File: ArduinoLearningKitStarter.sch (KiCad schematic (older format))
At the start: 83 parts, among them J1 USB_OTG, J10 DHT11, J2 CONN_01X08, J3 CONN_01X06, J4 CONN_01X08, J5 CONN_01X10, J6 I2C, J7 CONN_01X04, J8 CONN_01X02, J9 SPI, SW1 SW_PUSH, SW2 SW_PUSH, SW3 SW_PUSH, U1 arduino_nano, U2 arduino_uno, U3 ESP32-DEVKIT-C

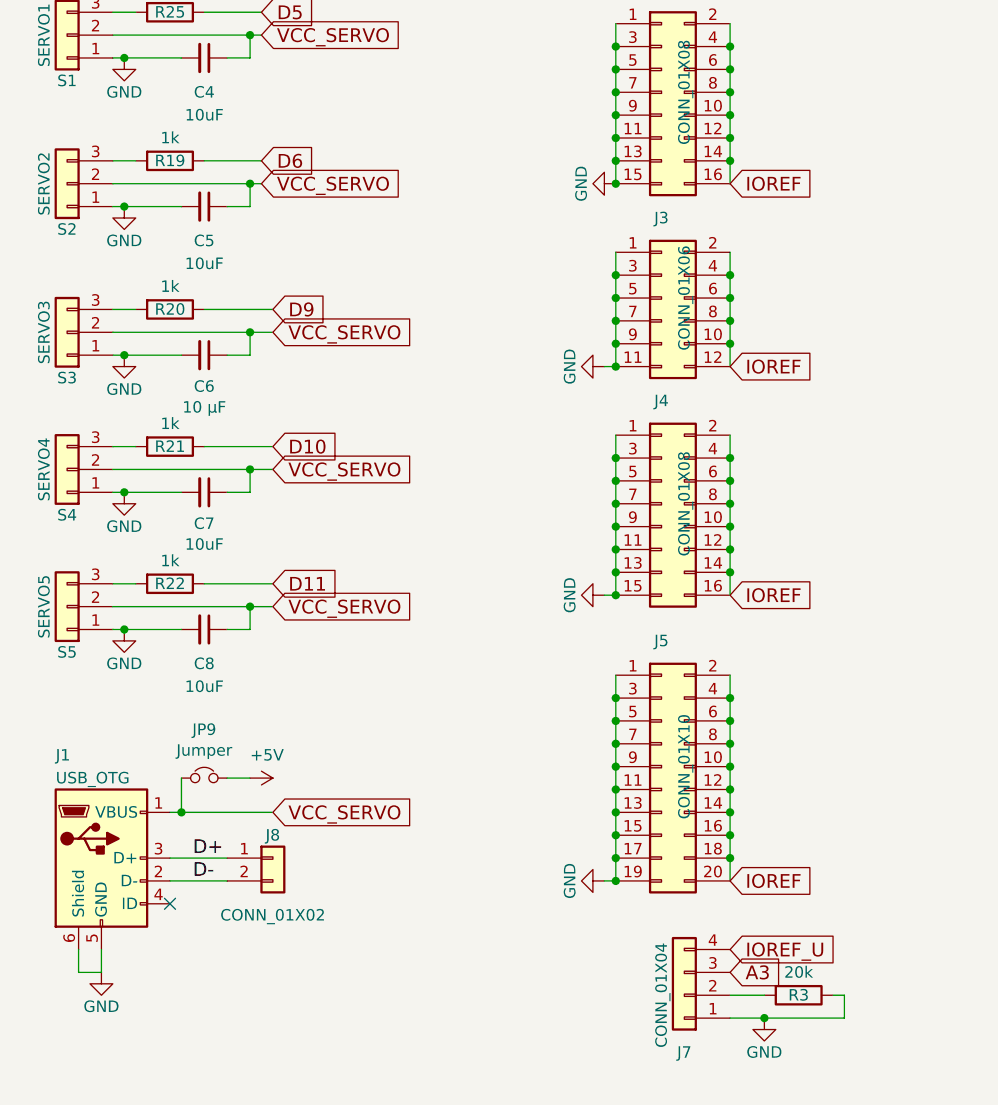
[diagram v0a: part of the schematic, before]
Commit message: Add connector for servo power supply
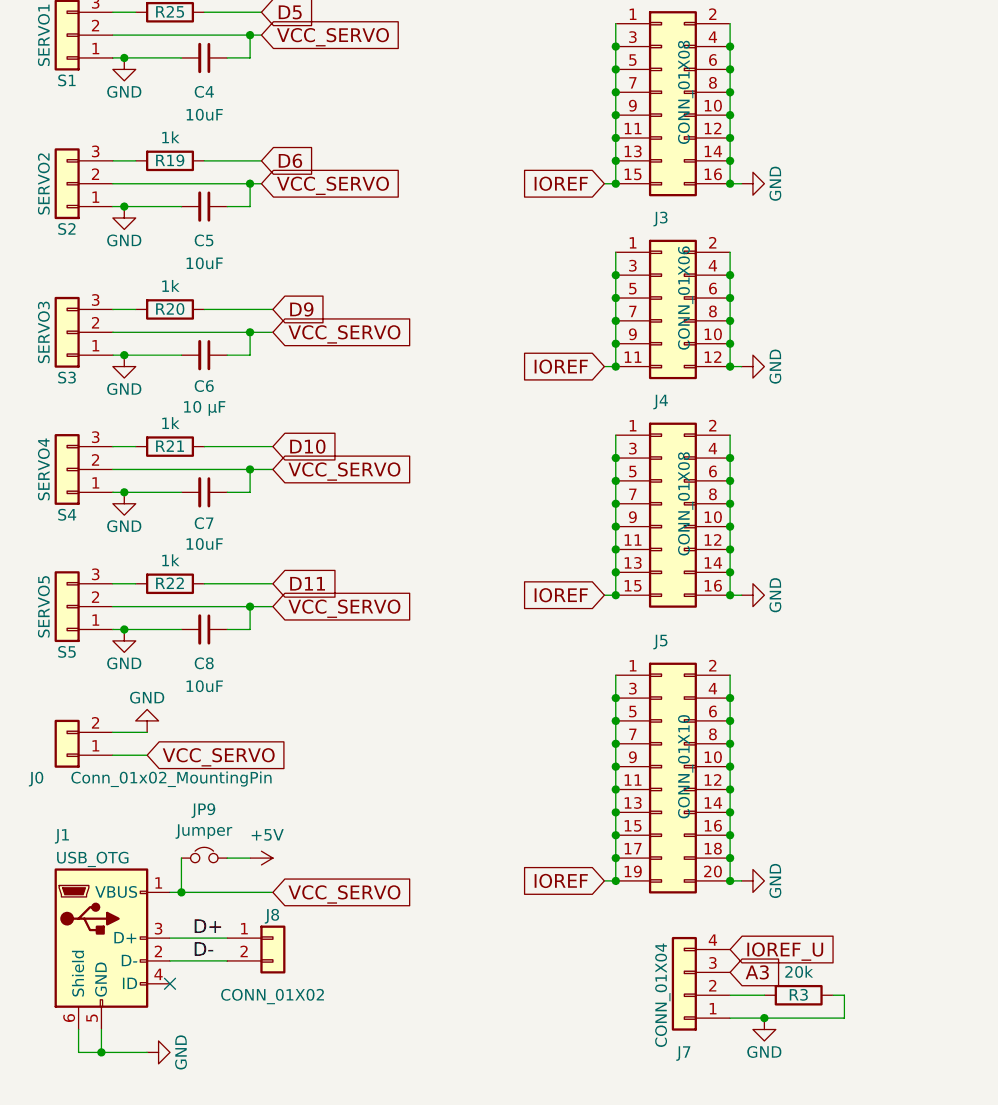
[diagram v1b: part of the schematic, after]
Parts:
- added J0: Conn_01x02_MountingPin, ALKS:2_pads_5mm, symbol ArduinoLearningKitStarter:Conn_01x02
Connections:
- net GND: now also J2.10 (Pin_10), J2.12 (Pin_12), J2.14 (Pin_14), J2.16 (Pin_16), J2.2 (Pin_2), J2.4 (Pin_4), J2.6 (Pin_6), J2.8 (Pin_8), J3.10 (Pin_10), J3.12 (Pin_12), J3.2 (Pin_2), J3.4 (Pin_4), J3.6 (Pin_6), J3.8 (Pin_8), J4.10 (Pin_10), J4.12 (Pin_12), J4.14 (Pin_14), J4.16 (Pin_16), J4.2 (Pin_2), J4.4 (Pin_4), J4.6 (Pin_6), J4.8 (Pin_8), J5.10 (Pin_10), J5.12 (Pin_12), J5.14 (Pin_14), J5.16 (Pin_16), J5.18 (Pin_18), J5.2 (Pin_2), J5.20 (Pin_20), J5.4 (Pin_4), J5.6 (Pin_6), J5.8 (Pin_8), J0.2 (Pin_2); no longer J2.1 (Pin_1), J2.11 (Pin_11), J2.13 (Pin_13), J2.15 (Pin_15), J2.3 (Pin_3), J2.5 (Pin_5), J2.7 (Pin_7), J2.9 (Pin_9), J3.1 (Pin_1), J3.11 (Pin_11), J3.3 (Pin_3), J3.5 (Pin_5), J3.7 (Pin_7), J3.9 (Pin_9), J4.1 (Pin_1), J4.11 (Pin_11), J4.13 (Pin_13), J4.15 (Pin_15), J4.3 (Pin_3), J4.5 (Pin_5), J4.7 (Pin_7), J4.9 (Pin_9), J5.1 (Pin_1), J5.11 (Pin_11), J5.13 (Pin_13), J5.15 (Pin_15), J5.17 (Pin_17), J5.19 (Pin_19), J5.3 (Pin_3), J5.5 (Pin_5), J5.7 (Pin_7), J5.9 (Pin_9)
- net IOREF: now also J2.1 (Pin_1), J2.11 (Pin_11), J2.13 (Pin_13), J2.15 (Pin_15), J2.3 (Pin_3), J2.5 (Pin_5), J2.7 (Pin_7), J2.9 (Pin_9), J3.1 (Pin_1), J3.11 (Pin_11), J3.3 (Pin_3), J3.5 (Pin_5), J3.7 (Pin_7), J3.9 (Pin_9), J4.1 (Pin_1), J4.11 (Pin_11), J4.13 (Pin_13), J4.15 (Pin_15), J4.3 (Pin_3), J4.5 (Pin_5), J4.7 (Pin_7), J4.9 (Pin_9), J5.1 (Pin_1), J5.11 (Pin_11), J5.13 (Pin_13), J5.15 (Pin_15), J5.17 (Pin_17), J5.19 (Pin_19), J5.3 (Pin_3), J5.5 (Pin_5), J5.7 (Pin_7), J5.9 (Pin_9); no longer J2.10 (Pin_10), J2.12 (Pin_12), J2.14 (Pin_14), J2.16 (Pin_16), J2.2 (Pin_2), J2.4 (Pin_4), J2.6 (Pin_6), J2.8 (Pin_8), J3.10 (Pin_10), J3.12 (Pin_12), J3.2 (Pin_2), J3.4 (Pin_4), J3.6 (Pin_6), J3.8 (Pin_8), J4.10 (Pin_10), J4.12 (Pin_12), J4.14 (Pin_14), J4.16 (Pin_16), J4.2 (Pin_2), J4.4 (Pin_4), J4.6 (Pin_6), J4.8 (Pin_8), J5.10 (Pin_10), J5.12 (Pin_12), J5.14 (Pin_14), J5.16 (Pin_16), J5.18 (Pin_18), J5.2 (Pin_2), J5.20 (Pin_20), J5.4 (Pin_4), J5.6 (Pin_6), J5.8 (Pin_8)
- net VCC_SERVO: now also J0.1 (Pin_1)
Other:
- moved on the sheet: J1, J8, JP9
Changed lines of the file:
@@
 L Connector:USB_B_Micro J1
 U 1 1 58C23B71
-P 1150 6750
-F 0 "J1" H 950 7200 50  0000 L CNN
-F 1 "USB_OTG" H 950 7100 50  0000 L CNN
-F 2 "yaqwsx:USB_Micro-B-widened" H 1300 6700 50  0001 C CNN
-F 3 "" H 1300 6700 50  0001 C CNN
-	1    1150 6750
-	1    0    0    -1
-$EndComp
-NoConn ~ 1450 6950
+P 1150 7100
+F 0 "J1" H 950 7550 50  0000 L CNN
+F 1 "USB_OTG" H 950 7450 50  0000 L CNN
+F 2 "yaqwsx:USB_Micro-B-widened" H 1300 7050 50  0001 C CNN
+F 3 "" H 1300 7050 50  0001 C CNN
+	1    1150 7100
+	1    0    0    -1
+$EndComp
+NoConn ~ 1450 7300
 $Comp
 L Device:R R25
@@
 L ArduinoLearningKitStarter:GND #PWR028
 U 1 1 58C2A0F7
-P 1150 7250
-F 0 "#PWR028" H 1150 7000 50  0001 C CNN
-F 1 "GND" H 1150 7100 50  0000 C CNN
-F 2 "" H 1150 7250 50  0000 C CNN
-F 3 "" H 1150 7250 50  0000 C CNN
-	1    1150 7250
-	1    0    0    -1
-$EndComp
-Text GLabel 1900 6550 2    60   Input ~ 0
+P 1350 7600
+F 0 "#PWR028" H 1350 7350 50  0001 C CNN
+F 1 "GND" H 1350 7450 50  0000 C CNN
+F 2 "" H 1350 7600 50  0000 C CNN
+F 3 "" H 1350 7600 50  0000 C CNN
+	1    1350 7600
+	0    -1   -1   0
+$EndComp
+Text GLabel 1900 6900 2    60   Input ~ 0
 VCC_SERVO
 $Comp
 L Device:Jumper_NC_Small JP9
 U 1 1 58C2CED2
-P 1600 6400
-F 0 "JP9" H 1600 6612 50  0000 C CNN
-F 1 "Jumper" H 1600 6521 50  0000 C CNN
-F 2 "Pin_Headers:Pin_Header_Straight_1x02" H 1600 6400 50  0001 C CNN
-F 3 "" H 1600 6400 50  0001 C CNN
-	1    1600 6400
+P 1600 6750
+F 0 "JP9" H 1600 6962 50  0000 C CNN
+F 1 "Jumper" H 1600 6871 50  0000 C CNN
+F 2 "Pin_Headers:Pin_Header_Straight_1x02" H 1600 6750 50  0001 C CNN
+F 3 "" H 1600 6750 50  0001 C CNN
+	1    1600 6750
 	-1   0    0    -1
 $EndComp
@@
 L ArduinoLearningKitStarter:+5V #PWR029
 U 1 1 58C30598
-P 1800 6400
-F 0 "#PWR029" H 1800 6250 50  0001 C CNN
-F 1 "+5V" V 1700 6400 50  0000 L CNN
-F 2 "" H 1800 6400 50  0000 C CNN
-F 3 "" H 1800 6400 50  0000 C CNN
-	1    1800 6400
+P 1800 6750
+F 0 "#PWR029" H 1800 6600 50  0001 C CNN
+F 1 "+5V" V 1700 6750 50  0000 L CNN
+F 2 "" H 1800 6750 50  0000 C CNN
+F 3 "" H 1800 6750 50  0000 C CNN
+	1    1800 6750
 	0    1    1    0
 $EndComp
@@
 $EndComp
 $Comp
-L ArduinoLearningKitStarter:GND #PWR031
-U 1 1 58C31560
-P 3350 4600
-F 0 "#PWR031" H 3350 4350 50  0001 C CNN
-F 1 "GND" H 3350 4450 50  0000 C CNN
-F 2 "" H 3350 4600 50  0000 C CNN
-F 3 "" H 3350 4600 50  0000 C CNN
-	1    3350 4600
-	0    1    1    0
-$EndComp
-$Comp
 L Connector_Generic:Conn_02x08_Odd_Even J4
 U 1 1 58C318EF
@@
 $EndComp
 $Comp
-L ArduinoLearningKitStarter:GND #PWR032
-U 1 1 58C319C6
-P 3350 5600
-F 0 "#PWR032" H 3350 5350 50  0001 C CNN
-F 1 "GND" H 3350 5450 50  0000 C CNN
-F 2 "" H 3350 5600 50  0000 C CNN
-F 3 "" H 3350 5600 50  0000 C CNN
-	1    3350 5600
-	0    1    1    0
-$EndComp
-$Comp
 L Connector_Generic:Conn_02x10_Odd_Even J5
 U 1 1 58C31A55
@@
 	1    0    0    -1
 $EndComp
-$Comp
-L ArduinoLearningKitStarter:GND #PWR033
-U 1 1 58C326A3
-P 3350 6850
-F 0 "#PWR033" H 3350 6600 50  0001 C CNN
-F 1 "GND" H 3350 6700 50  0000 C CNN
-F 2 "" H 3350 6850 50  0000 C CNN
-F 3 "" H 3350 6850 50  0000 C CNN
-	1    3350 6850
-	0    1    1    0
-$EndComp
 Text GLabel 7950 1300 0    60   Input ~ 0
 IOREF
-$Comp
-L ArduinoLearningKitStarter:GND #PWR034
-U 1 1 58C335CF
-P 3400 3800
-F 0 "#PWR034" H 3400 3550 50  0001 C CNN
-F 1 "GND" H 3400 3650 50  0000 C CNN
-F 2 "" H 3400 3800 50  0000 C CNN
-F 3 "" H 3400 3800 50  0000 C CNN
-	1    3400 3800
-	0    1    1    0
-$EndComp
 $Comp
 L ArduinoLearningKitStarter:GND #PWR037
@@
 L Connector_Generic:Conn_01x02 J8
 U 1 1 5905E2A7
-P 1900 6750
-F 0 "J8" H 1900 6850 50  0000 C CNN
-F 1 "CONN_01X02" H 1900 6500 50  0000 C CNN
-F 2 "Connector_PinHeader_2.54mm:PinHeader_1x02_P2.54mm_Vertical" H 1900 6750 50  0001 C CNN
-F 3 "" H 1900 6750 50  0001 C CNN
-	1    1900 6750
+P 1900 7100
+F 0 "J8" H 1900 7200 50  0000 C CNN
+F 1 "CONN_01X02" H 1900 6850 50  0000 C CNN
+F 2 "Connector_PinHeader_2.54mm:PinHeader_1x02_P2.54mm_Vertical" H 1900 7100 50  0001 C CNN
+F 3 "" H 1900 7100 50  0001 C CNN
+	1    1900 7100
 	1    0    0    -1
 $EndComp
@@
 	1100 1100 1100 1200
 Wire Wire Line
-	1050 7150 1050 7250
-Wire Wire Line
-	1050 7250 1150 7250
-Wire Wire Line
-	1150 7250 1150 7150
-Wire Wire Line
-	1450 6550 1500 6550
+	1050 7500 1050 7600
+Wire Wire Line
+	1050 7600 1150 7600
+Wire Wire Line
+	1150 7600 1150 7500
+Wire Wire Line
+	1450 6900 1500 6900
 Wire Wire Line
 	3900 7450 4050 7450
@@
 	10500 5250 10750 5250
 Wire Wire Line
-	1450 6750 1700 6750
-Wire Wire Line
-	1450 6850 1700 6850
-Text Label 1550 6750 0    60   ~ 0
+	1450 7100 1700 7100
+Wire Wire Line
+	1450 7200 1700 7200
+Text Label 1550 7100 0    60   ~ 0
 D+
-Text Label 1550 6850 0    60   ~ 0
+Text Label 1550 7200 0    60   ~ 0
 D-
 $Comp
@@
 	4050 7450 4400 7450
 Wire Wire Line
-	1500 6550 1900 6550
-Connection ~ 1500 6550
-Wire Wire Line
-	1500 6400 1500 6550
-Wire Wire Line
-	1700 6400 1800 6400
+	1500 6900 1900 6900
+Connection ~ 1500 6900
+Wire Wire Line
+	1500 6750 1500 6900
+Wire Wire Line
+	1700 6750 1800 6750
 Wire Wire Line
 	6450 6950 6450 7050
@@
 Wire Wire Line
 	3400 5000 3400 5100
-Text GLabel 3900 3800 2    60   Input ~ 0
-IOREF
-Text GLabel 3900 4600 2    60   Input ~ 0
-IOREF
-Text GLabel 3900 5600 2    60   Input ~ 0
-IOREF
-Text GLabel 3900 6850 2    60   Input ~ 0
-IOREF
 Wire Wire Line
 	3400 3500 3400 3400
@@
 	3400 3200 3400 3100
 Connection ~ 3400 3200
-Connection ~ 3400 3800
 Wire Wire Line
 	3900 3100 3900 3200
@@
 Connection ~ 3900 6150
 Connection ~ 3900 6050
+$Comp
+L ArduinoLearningKitStarter:Conn_01x02 J0
+U 1 1 5C44376C
+P 1000 6300
+F 0 "J0" H 1100 6400 50  0000 L CNN
+F 1 "Conn_01x02_MountingPin" H 100 6400 50  0000 L CNN
+F 2 "ALKS:2_pads_5mm" H 1000 6300 50  0001 C CNN
+F 3 "~" H 1000 6300 50  0001 C CNN
+	1    1000 6300
+	-1   0    0    1
+$EndComp
+Wire Wire Line
+	1150 7600 1350 7600
+Connection ~ 1150 7600
+Text GLabel 1350 6300 2    60   Input ~ 0
+VCC_SERVO
+$Comp
+L ArduinoLearningKitStarter:GND #PWR0102
+U 1 1 5C5AF723
+P 1350 6200
+F 0 "#PWR0102" H 1350 5950 50  0001 C CNN
+F 1 "GND" H 1350 6050 50  0000 C CNN
+F 2 "" H 1350 6200 50  0000 C CNN
+F 3 "" H 1350 6200 50  0000 C CNN
+	1    1350 6200
+	-1   0    0    1
+$EndComp
+Wire Wire Line
+	1200 6200 1350 6200
+Wire Wire Line
+	1350 6300 1200 6300
+Text GLabel 3350 3800 0    60   Input ~ 0
+IOREF
+Text GLabel 3350 4600 0    60   Input ~ 0
+IOREF
+Text GLabel 3350 5600 0    60   Input ~ 0
+IOREF
+Text GLabel 3350 6850 0    60   Input ~ 0
+IOREF
+$Comp
+L ArduinoLearningKitStarter:GND #PWR0103
+U 1 1 5C618097
+P 3950 3800
+F 0 "#PWR0103" H 3950 3550 50  0001 C CNN
+F 1 "GND" H 3950 3650 50  0000 C CNN
+F 2 "" H 3950 3800 50  0000 C CNN
+F 3 "" H 3950 3800 50  0000 C CNN
+	1    3950 3800
+	0    -1   -1   0
+$EndComp
+$Comp
+L ArduinoLearningKitStarter:GND #PWR0104
+U 1 1 5C618246
+P 3950 4600
+F 0 "#PWR0104" H 3950 4350 50  0001 C CNN
+F 1 "GND" H 3950 4450 50  0000 C CNN
+F 2 "" H 3950 4600 50  0000 C CNN
+F 3 "" H 3950 4600 50  0000 C CNN
+	1    3950 4600
+	0    -1   -1   0
+$EndComp
+$Comp
+L ArduinoLearningKitStarter:GND #PWR0105
+U 1 1 5C6182F9
+P 3950 5600
+F 0 "#PWR0105" H 3950 5350 50  0001 C CNN
+F 1 "GND" H 3950 5450 50  0000 C CNN
+F 2 "" H 3950 5600 50  0000 C CNN
+F 3 "" H 3950 5600 50  0000 C CNN
+	1    3950 5600
+	0    -1   -1   0
+$EndComp
+$Comp
+L ArduinoLearningKitStarter:GND #PWR0106
+U 1 1 5C6183AC
+P 3950 6850
+F 0 "#PWR0106" H 3950 6600 50  0001 C CNN
+F 1 "GND" H 3950 6700 50  0000 C CNN
+F 2 "" H 3950 6850 50  0000 C CNN
+F 3 "" H 3950 6850 50  0000 C CNN
+	1    3950 6850
+	0    -1   -1   0
+$EndComp
+Wire Wire Line
+	3950 6850 3900 6850
+Connection ~ 3900 6850
+Wire Wire Line
+	3950 5600 3900 5600
+Connection ~ 3900 5600
+Wire Wire Line
+	3950 4600 3900 4600
+Connection ~ 3900 4600
+Wire Wire Line
+	3350 3800 3400 3800
+Connection ~ 3400 3800
+Wire Wire Line
+	3900 3800 3950 3800
+Connection ~ 3900 3800
 $EndSCHEMATC
